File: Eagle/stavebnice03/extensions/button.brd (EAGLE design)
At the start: 4 parts

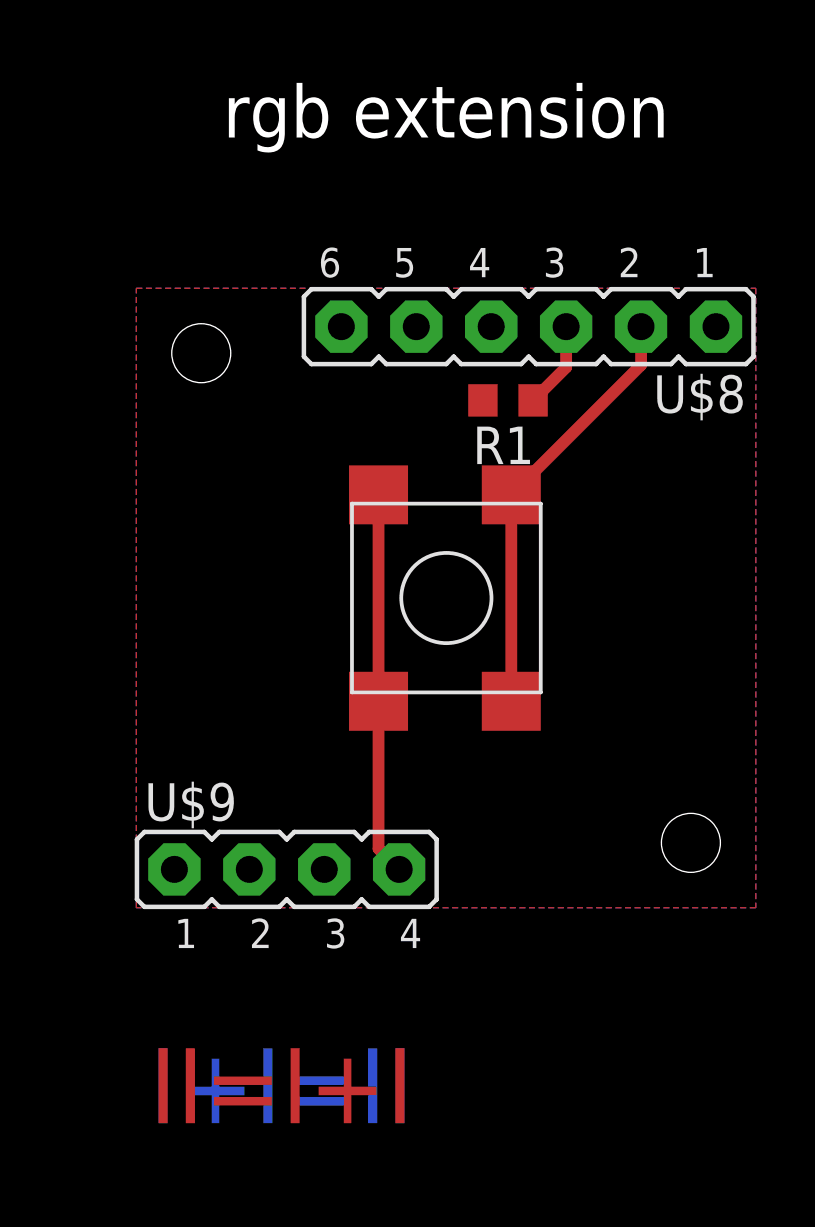
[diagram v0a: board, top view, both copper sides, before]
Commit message: eagle adjustment for the Jíťa version
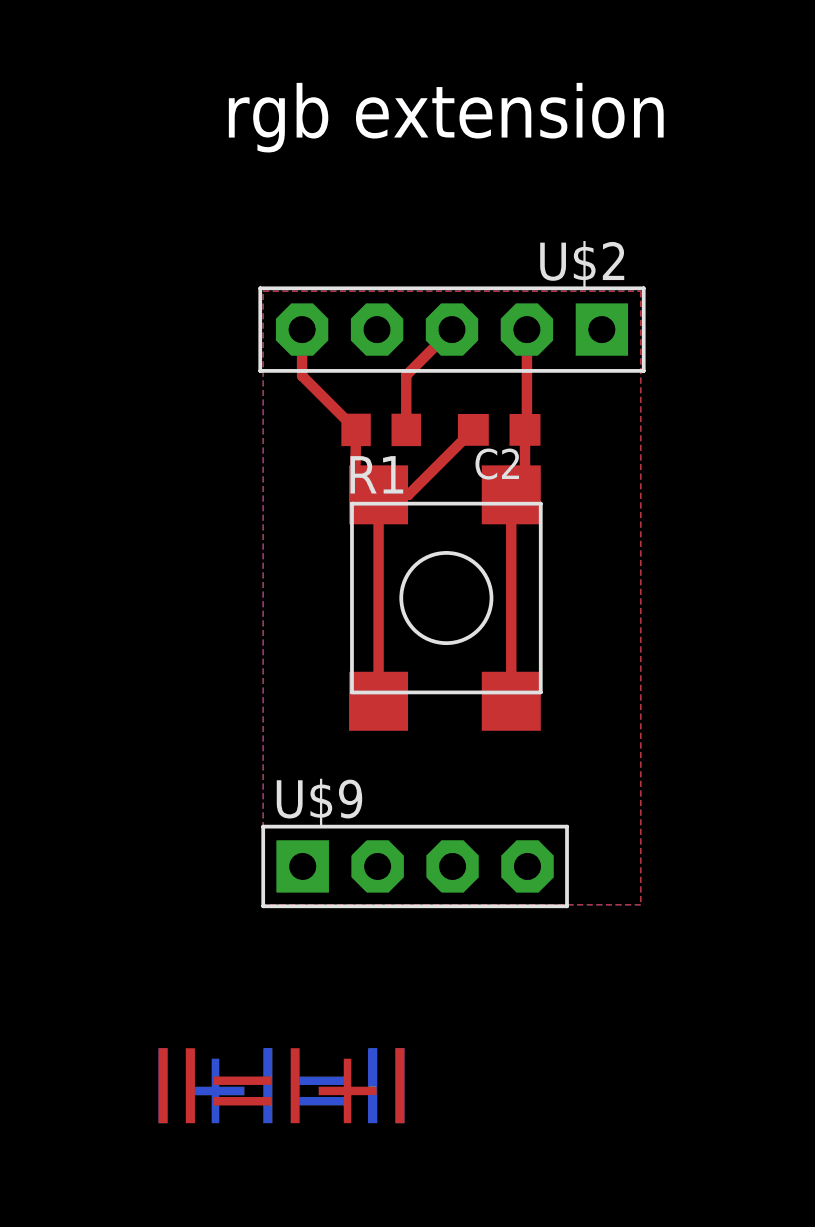
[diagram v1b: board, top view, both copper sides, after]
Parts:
- removed U$8: JUMPER6M, !stavebnice03:JUMPER6M
- added C2: 100nF, resistor:C0603K
- added U$2: JUMPER5M, !stavebnice03:JUMPER5M
- moved R1 4.41 mm to (8.30, 16.2)
- moved U$9 4.35 mm to (9.45, 1.40)
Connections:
- removed net N$2: U$1.P$1, U$1.P$3, U$8.2
- removed net N$3: R1.1, U$8.3
- new net AA: C2.2, R1.2, U$1.P$2, U$1.P$4, U$2.5
- new net VCC: C2.1, U$1.P$1, U$1.P$3, U$2.2
- net GND: now also R1.1, U$2.3, U$9.1, U$9.2, U$9.3; no longer R1.2, U$1.P$2, U$1.P$4
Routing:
- net AA: track 0.00 -> 18.5 mm
- net N$2: track 14.5 -> 0.00 mm
- net VCC: track 0.00 -> 12.8 mm
- net GND: track 13.0 -> 4.04 mm
- net N$3: track 2.96 -> 0.00 mm
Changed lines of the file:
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@@
 <layers>
 <layer number="1" name="Top" color="4" fill="1" visible="yes" active="yes"/>
-<layer number="16" name="Bottom" color="1" fill="1" visible="no" active="yes"/>
+<layer number="16" name="Bottom" color="1" fill="1" visible="yes" active="yes"/>
 <layer number="17" name="Pads" color="2" fill="1" visible="yes" active="yes"/>
 <layer number="18" name="Vias" color="2" fill="1" visible="yes" active="yes"/>
@@
 <layer number="20" name="Dimension" color="15" fill="1" visible="yes" active="yes"/>
 <layer number="21" name="tPlace" color="7" fill="1" visible="yes" active="yes"/>
-<layer number="22" name="bPlace" color="7" fill="1" visible="no" active="yes"/>
+<layer number="22" name="bPlace" color="7" fill="1" visible="yes" active="yes"/>
 <layer number="23" name="tOrigins" color="15" fill="1" visible="yes" active="yes"/>
-<layer number="24" name="bOrigins" color="15" fill="1" visible="no" active="yes"/>
+<layer number="24" name="bOrigins" color="15" fill="1" visible="yes" active="yes"/>
 <layer number="25" name="tNames" color="7" fill="1" visible="no" active="yes"/>
 <layer number="26" name="bNames" color="7" fill="1" visible="no" active="yes"/>
@@
 <layer number="42" name="bRestrict" color="1" fill="10" visible="no" active="yes"/>
 <layer number="43" name="vRestrict" color="2" fill="10" visible="no" active="yes"/>
-<layer number="44" name="Drills" color="7" fill="1" visible="no" active="yes"/>
-<layer number="45" name="Holes" color="7" fill="1" visible="no" active="yes"/>
+<layer number="44" name="Drills" color="7" fill="1" visible="yes" active="yes"/>
+<layer number="45" name="Holes" color="7" fill="1" visible="yes" active="yes"/>
 <layer number="46" name="Milling" color="3" fill="1" visible="no" active="yes"/>
 <layer number="47" name="Measures" color="7" fill="1" visible="no" active="yes"/>
 <layer number="48" name="Document" color="7" fill="1" visible="no" active="yes"/>
 <layer number="49" name="Reference" color="7" fill="1" visible="yes" active="yes"/>
-<layer number="51" name="tDocu" color="7" fill="1" visible="no" active="yes"/>
-<layer number="52" name="bDocu" color="7" fill="1" visible="no" active="yes"/>
+<layer number="51" name="tDocu" color="7" fill="1" visible="yes" active="yes"/>
+<layer number="52" name="bDocu" color="7" fill="1" visible="yes" active="yes"/>
 <layer number="90" name="Modules" color="5" fill="1" visible="no" active="no"/>
 <layer number="91" name="Nets" color="2" fill="1" visible="no" active="no"/>
@@
 <board>
 <plain>
-<hole x="2.2" y="18.8" drill="2"/>
-<hole x="18.8" y="2.2" drill="2"/>
 <text x="4.92125" y="-6.0325" size="2.54" layer="16" rot="MR0" align="center">II=I+I</text>
 <text x="4.92125" y="-6.0325" size="2.54" layer="1" align="center">II=I+I</text>
@@
 <circle x="6.37" y="1.3" radius="0.329" width="0.357" layer="116"/>
 <circle x="8.91" y="1.3" radius="0.329" width="0.357" layer="116"/>
-<wire x1="0" y1="0" x2="0" y2="21" width="0.0762" layer="49"/>
-<wire x1="0" y1="21" x2="21" y2="21" width="0.0762" layer="49"/>
-<wire x1="21" y1="21" x2="21" y2="0" width="0.0762" layer="49"/>
-<wire x1="21" y1="0" x2="0" y2="0" width="0.0762" layer="49"/>
+<wire x1="4.2" y1="0" x2="4.2" y2="21" width="0.0762" layer="49"/>
+<wire x1="4.2" y1="21" x2="17.2" y2="21" width="0.0762" layer="49"/>
+<wire x1="17.2" y1="21" x2="17.2" y2="0" width="0.0762" layer="49"/>
+<wire x1="17.2" y1="0" x2="4.2" y2="0" width="0.0762" layer="49"/>
 <wire x1="-10" y1="-10" x2="-2.5" y2="-10" width="0.01" layer="49"/>
 <wire x1="-2.5" y1="-10" x2="23.5" y2="-10" width="0.01" layer="49"/>
@@
 </autorouter>
 <elements>
-<element name="U$8" library="!stavebnice03" package="JUMPER6M" value="JUMPER6M" x="13.3" y="19.7" rot="R180"/>
-<element name="U$9" library="!stavebnice03" package="JUMPER4M" value="JUMPER4M" x="5.1" y="1.3"/>
-<element name="R1" library="resistor" package="R0603" value="100k" x="12.6" y="17.2" rot="R180"/>
+<element name="U$9" library="!stavebnice03" package="JUMPER4M" value="JUMPER4M" x="9.45" y="1.4"/>
+<element name="R1" library="resistor" package="R0603" value="100k" x="8.3" y="16.2" rot="R180"/>
 <element name="U$1" library="!stavebnice03" package="BUTTON_6.2X6.2" value="BUTTON_6.3X6.3" x="10.5" y="10.5" rot="R180"/>
+<element name="U$2" library="!stavebnice03" package="JUMPER5M" value="JUMPER5M" x="10.7" y="19.6" rot="R180"/>
+<element name="C2" library="resistor" package="C0603K" value="100nF" x="12.3" y="16.2" rot="R180"/>
 </elements>
 <signals>
-<signal name="GND">
-<polygon width="0.01" layer="1" isolate="0.4826" thermals="no" rank="2">
-<vertex x="0" y="0"/>
-<vertex x="0" y="21"/>
-<vertex x="21" y="21"/>
-<vertex x="21" y="0"/>
-</polygon>
-<polygon width="0.05" layer="16" isolate="0.4064" thermals="no" rank="2">
-<vertex x="0" y="0"/>
-<vertex x="0" y="21"/>
-<vertex x="21" y="21"/>
-<vertex x="21" y="0"/>
-</polygon>
+<signal name="AA">
 <contactref element="U$1" pad="P$4"/>
 <contactref element="U$1" pad="P$2"/>
 <contactref element="R1" pad="2"/>
-<contactref element="U$9" pad="4"/>
-<wire x1="8.21" y1="14" x2="8.21" y2="2" width="0.4" layer="1"/>
-<wire x1="8.21" y1="2" x2="8.91" y2="1.3" width="0.4" layer="1"/>
-<wire x1="8.25" y1="14.04" x2="8.21" y2="14" width="0.4" layer="1"/>
+<contactref element="C2" pad="2"/>
+<wire x1="8.21" y1="7" x2="8.21" y2="14" width="0.3556" layer="1"/>
+<wire x1="8.21" y1="14" x2="7.41" y2="14.06" width="0.3556" layer="1"/>
+<wire x1="7.41" y1="14.06" x2="7.45" y2="16.2" width="0.3556" layer="1"/>
+<contactref element="U$2" pad="5"/>
+<wire x1="5.62" y1="19.6" x2="5.62" y2="18.03" width="0.3556" layer="1"/>
+<wire x1="5.62" y1="18.03" x2="7.45" y2="16.2" width="0.3556" layer="1"/>
+<wire x1="8.5" y1="7" x2="8.21" y2="7" width="0.3556" layer="1"/>
+<wire x1="9.225" y1="14" x2="8.21" y2="14" width="0.3556" layer="1"/>
+<wire x1="11.425" y1="16.2" x2="9.225" y2="14" width="0.3556" layer="1"/>
 </signal>
 <signal name="N$19">
 </signal>
-<signal name="N$2">
-<contactref element="U$8" pad="2"/>
+<signal name="GND">
+<contactref element="R1" pad="1"/>
+<contactref element="U$2" pad="3"/>
+<polygon width="0.2" layer="16" isolate="0.4064" thermals="no" rank="2">
+<vertex x="4.3" y="0.1"/>
+<vertex x="4.3" y="20.9"/>
+<vertex x="17.1" y="20.9"/>
+<vertex x="17.1" y="0.1"/>
+</polygon>
+<polygon width="0.2" layer="1" isolate="0.4064" thermals="no" rank="2">
+<vertex x="4.3" y="0.1"/>
+<vertex x="4.3" y="20.9"/>
+<vertex x="17.1" y="20.9"/>
+<vertex x="17.1" y="0.1"/>
+</polygon>
+<wire x1="9.15" y1="16.2" x2="9.15" y2="18.05" width="0.3556" layer="1"/>
+<wire x1="9.15" y1="18.05" x2="10.7" y2="19.6" width="0.3556" layer="1"/>
+<contactref element="U$9" pad="2"/>
+<contactref element="U$9" pad="3"/>
+<contactref element="U$9" pad="4"/>
+<contactref element="U$9" pad="1"/>
+</signal>
+<signal name="VCC">
+<contactref element="C2" pad="1"/>
+<contactref element="U$2" pad="2"/>
 <contactref element="U$1" pad="P$3"/>
 <contactref element="U$1" pad="P$1"/>
-<wire x1="17.11" y1="19.7" x2="17.11" y2="18.4" width="0.4" layer="1"/>
-<wire x1="17.11" y1="18.4" x2="12.71" y2="14" width="0.4" layer="1"/>
-<wire x1="12.71" y1="14" x2="12.71" y2="7" width="0.4" layer="1"/>
-</signal>
-<signal name="N$3">
-<contactref element="R1" pad="1"/>
-<contactref element="U$8" pad="3"/>
-<wire x1="14.57" y1="19.7" x2="14.57" y2="18.32" width="0.4" layer="1"/>
-<wire x1="14.57" y1="18.32" x2="13.45" y2="17.2" width="0.4" layer="1"/>
+<wire x1="12.71" y1="14" x2="12.71" y2="7" width="0.3556" layer="1"/>
+<wire x1="13.24" y1="19.6" x2="13.24" y2="16.265" width="0.3556" layer="1"/>
+<wire x1="13.24" y1="16.265" x2="13.175" y2="16.2" width="0.3556" layer="1"/>
+<wire x1="13.175" y1="16.2" x2="13.175" y2="14.465" width="0.3556" layer="1"/>
+<wire x1="13.175" y1="14.465" x2="12.71" y2="14" width="0.3556" layer="1"/>
 </signal>
 </signals>
